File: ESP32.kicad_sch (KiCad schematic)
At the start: 29 parts, among them J1 USB_B_Micro, J2 BATT, J3 PMS7003 Connector, J4 BootSel, J5 UART, Q1 AO3401A, SW1 RESET, U1 ESP32-C3-MINI-1, U2 AMS1117-3.3, U3 AMS1117-5.0

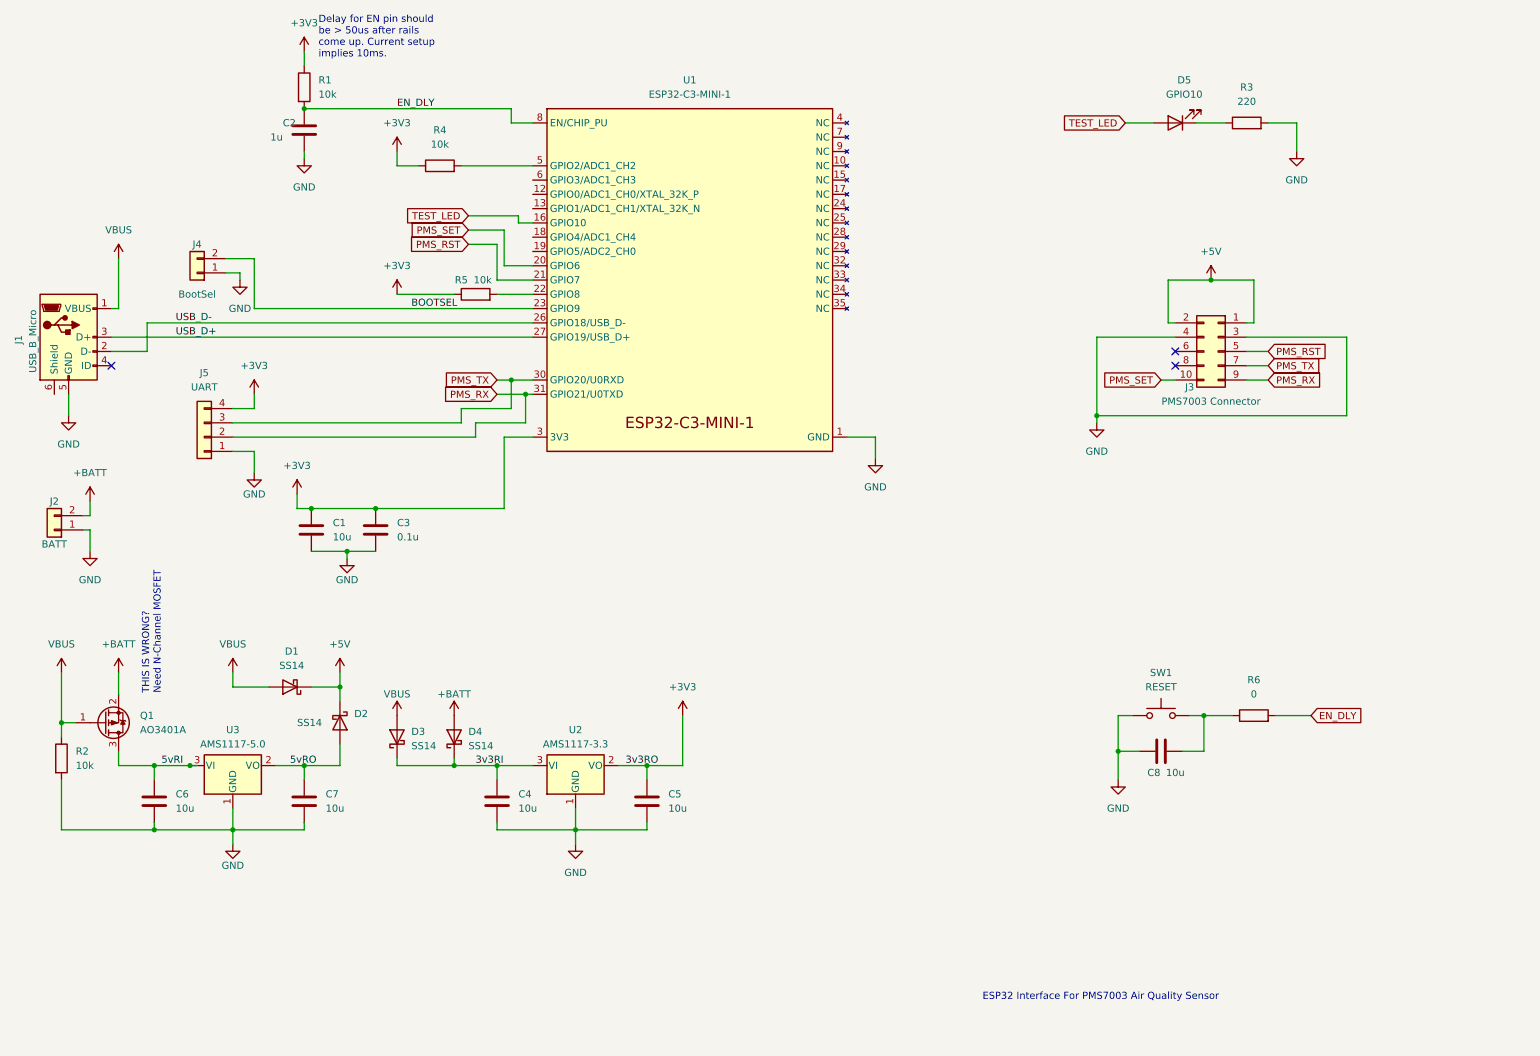
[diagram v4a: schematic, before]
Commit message: Sch layout + reroute
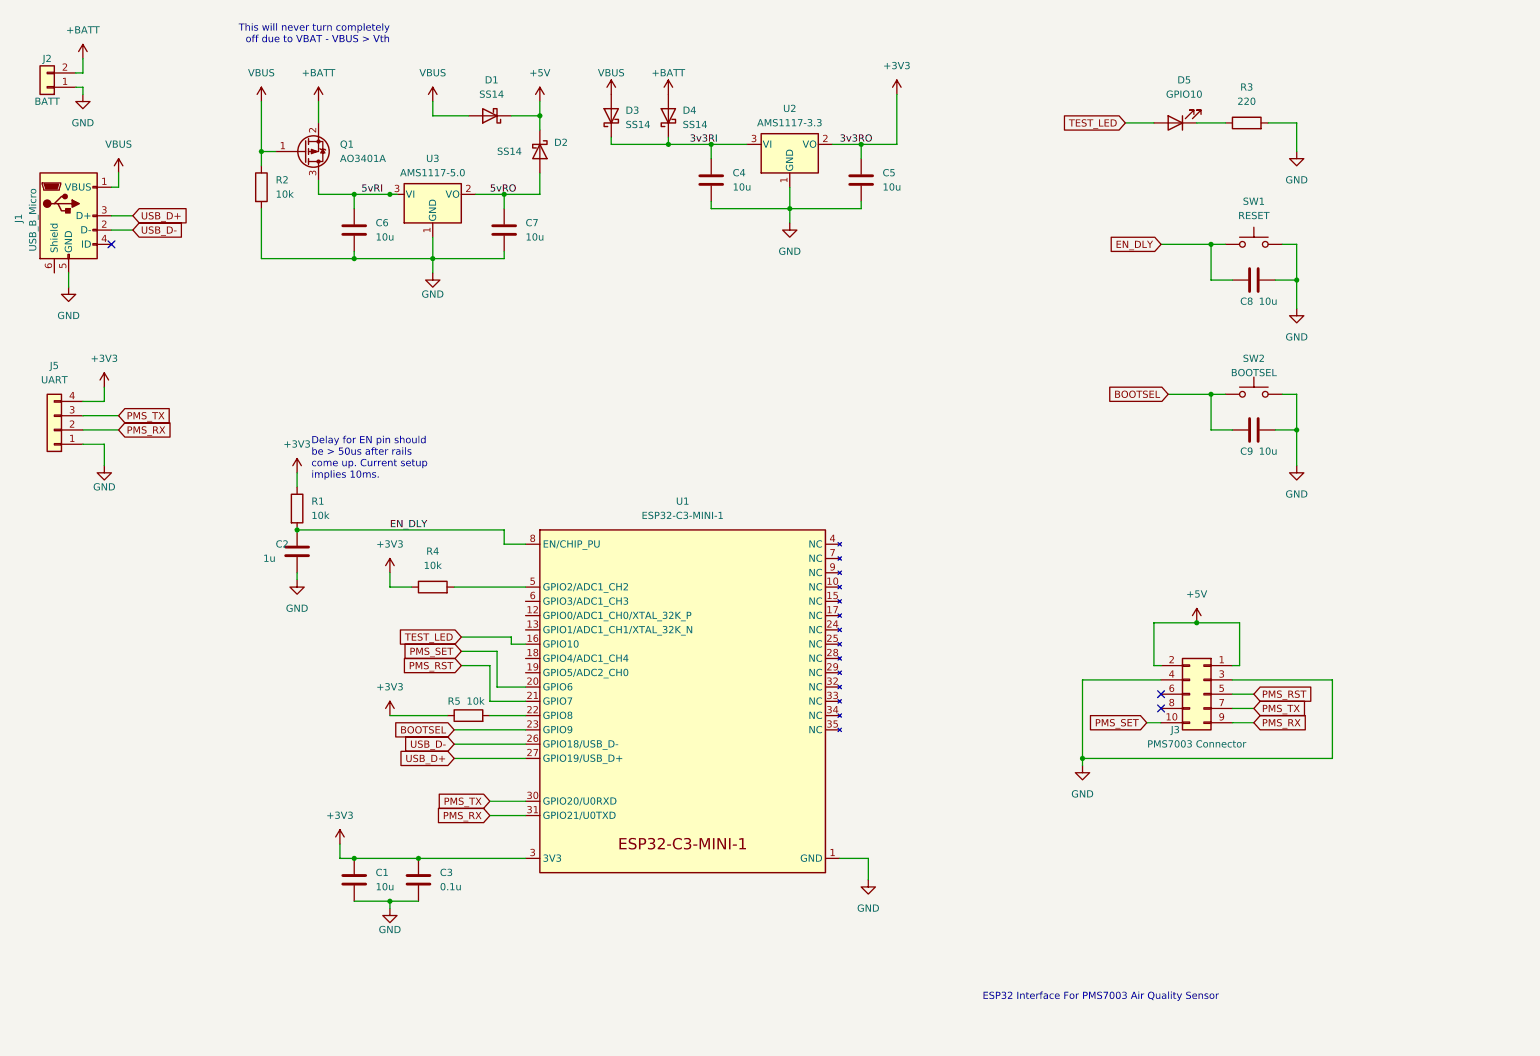
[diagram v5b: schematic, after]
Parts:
- removed J4: BootSel, Connector_PinHeader_2.54mm:PinHeader_1x02_P2.54mm_Vertical, symbol Connector_Generic:Conn_01x02
- removed R6: 0, Resistor_SMD:R_0603_1608Metric_Pad0.98x0.95mm_HandSolder, symbol Device:R
- added C9: 10u, Capacitor_SMD:C_0603_1608Metric_Pad1.08x0.95mm_HandSolder, symbol Device:C
- added SW2: BOOTSEL, Button_Switch_SMD:SW_Push_1P1T_NO_Vertical_Wuerth_434133025816, symbol Switch:SW_Push
- J2: footprint Connector_PinHeader_2.54mm:PinHeader_1x02_P2.54mm_Vertical -> Connector_PinHeader_2.54mm:PinHeader_1x02_P2.54mm_Vertical_SMD_Pin1Right
- J5: footprint Connector_PinHeader_2.54mm:PinHeader_1x04_P2.54mm_Vertical -> Connector_PinHeader_2.54mm:PinHeader_1x04_P2.54mm_Vertical_SMD_Pin1Right
- SW1: footprint Button_Switch_THT:SW_PUSH_6mm -> Button_Switch_SMD:SW_Push_1P1T_NO_Vertical_Wuerth_434133025816
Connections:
- net BOOTSEL: now also C9.1, SW2.1
- net EN_DLY: now also C8.1, SW1.1
- net GND: now also C8.2, SW1.2, C9.2, SW2.2; no longer C8.1, SW1.1
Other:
- note added: "This will never turn completely off due to VBAT - VBUS > Vth"
- note removed: "THIS IS WRONG? Need N-Channel MOSFET"
- moved on the sheet: C1, C2, C3, C4, C5, C6, C7, C8, D1, D2, D3, D4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

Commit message: Replaced linear regulators with buck converters
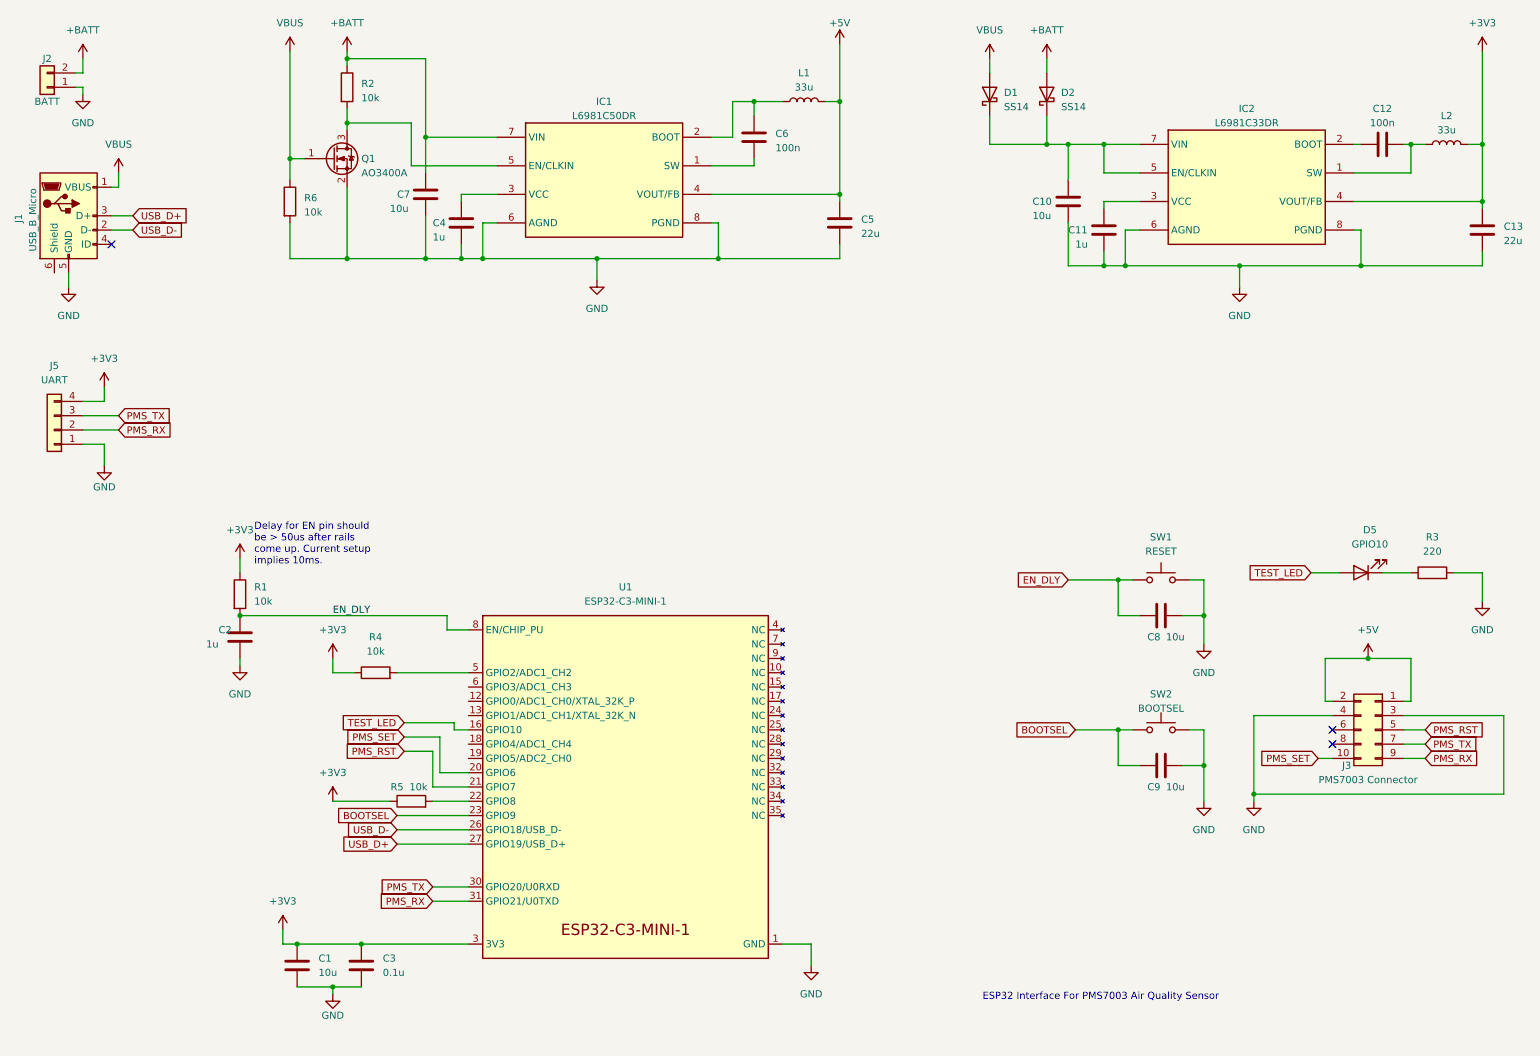
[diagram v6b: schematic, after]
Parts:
- removed D3, D4: SS14, Diode_SMD:D_SMA_Handsoldering, symbol Device:D_Schottky
- removed Q1: AO3401A, Package_TO_SOT_SMD:SOT-23, symbol Transistor_FET:AO3401A
- removed U2: AMS1117-3.3, Package_TO_SOT_SMD:SOT-223-3_TabPin2, symbol Regulator_Linear:AMS1117-3.3
- removed U3: AMS1117-5.0, Package_TO_SOT_SMD:SOT-223-3_TabPin2, symbol Regulator_Linear:AMS1117-5.0
- added C10: 10u, Capacitor_SMD:C_0603_1608Metric_Pad1.08x0.95mm_HandSolder, symbol Device:C
- added C11: 1u, Capacitor_SMD:C_0603_1608Metric_Pad1.08x0.95mm_HandSolder, symbol Device:C
- added C12: 100n, Capacitor_SMD:C_0603_1608Metric_Pad1.08x0.95mm_HandSolder, symbol Device:C
- added C13: 22u, Capacitor_SMD:C_0603_1608Metric_Pad1.08x0.95mm_HandSolder, symbol Device:C
- added IC1: L6981C50DR, DC Converters:SOIC127P600X175-8N, symbol L6981C50DR:L6981C50DR
- added IC2: L6981C33DR, DC Converters:SOIC127P600X175-8N, symbol L6981C50DR:L6981C33DR
- added L1, L2: 33u, Inductor_SMD:L_Murata_29xxxC, symbol Device:L
- added Q1: AO3400A, Package_TO_SOT_SMD:SOT-23, symbol Transistor_FET:AO3400A
- added R6: 10k, Resistor_SMD:R_0603_1608Metric_Pad0.98x0.95mm_HandSolder, symbol Device:R
- C4: value 10u -> 1u; footprint Capacitor_SMD:C_1206_3216Metric_Pad1.33x1.80mm_HandSolder -> Capacitor_SMD:C_0603_1608Metric_Pad1.08x0.95mm_HandSolder
- C5: value 10u -> 22u; footprint Capacitor_Tantalum_SMD:CP_EIA-3216-18_Kemet-A_Pad1.58x1.35mm_HandSolder -> Capacitor_SMD:C_0603_1608Metric_Pad1.08x0.95mm_HandSolder
- C6: value 10u -> 100n; footprint Capacitor_SMD:C_1206_3216Metric_Pad1.33x1.80mm_HandSolder -> Capacitor_SMD:C_0603_1608Metric_Pad1.08x0.95mm_HandSolder
- C7: footprint Capacitor_Tantalum_SMD:CP_EIA-3216-18_Kemet-A_Pad1.58x1.35mm_HandSolder -> Capacitor_SMD:C_0603_1608Metric_Pad1.08x0.95mm_HandSolder
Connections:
- net 5vRO is gone; now on net +BATT: C7.1, D2.2 (A)
- net +3V3: now also C13.1, IC2.4 (VOUT/FB), L2.2; no longer C5.1
- net +5V: now also C5.1, IC1.4 (VOUT/FB), L1.2; no longer D1.1 (K), D2.1 (K)
- net +BATT: now also R2.1, IC1.7 (VIN)
- net GND: now also C10.2, C11.2, C13.2, IC1.6 (AGND), IC1.8 (PGND), IC2.6 (AGND), IC2.8 (PGND), Q1.2 (S), R6.2; no longer C6.2, R2.2
- net VBUS: now also Q1.1 (G), R6.1; no longer R2.1
- net 3v3RI: no longer names the net of C4.1
- net 3v3RI: now also IC1.3 (VCC)
- net 5vRI: no longer names the net of C6.1
- net 5vRI: now also IC1.1 (SW)
- new net: IC1.5 (EN/CLKIN), Q1.3 (D), R2.2
- new net: C10.1, D1.1 (K), D2.1 (K), IC2.5 (EN/CLKIN), IC2.7 (VIN)
- new net: C6.2, IC1.2 (BOOT), L1.1
- new net: C12.2, IC2.1 (SW), L2.1
- new net: C12.1, IC2.2 (BOOT)
- new net: C11.1, IC2.3 (VCC)
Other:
- note removed: "This will never turn completely off due to VBAT - VBUS > Vth"
- moved on the sheet: C1, C2, C3, C8, C9, D5, J3, R1, R3, R4, R5, SW1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

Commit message: Schematic + Layout
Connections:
- net PMS_RX: now also J3.7 (Pin_7); no longer J3.9 (Pin_9)
- net PMS_TX: now also J3.9 (Pin_9); no longer J3.7 (Pin_7)
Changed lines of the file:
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@@
+    (stroke (width 0) (type default))
+  )
+  (wire (pts (xy 261.62 147.32) (xy 265.43 147.32))
     (stroke (width 0) (type default))
   )
@@
     (stroke (width 0) (type default))
   )
-  (wire (pts (xy 261.62 147.32) (xy 265.43 147.32))
-    (stroke (width 0) (type default))
-  )
   (wire (pts (xy 71.12 132.08) (xy 74.93 132.08))
     (stroke (width 0) (type default))
@@
     (stroke (width 0) (type default))
   )
+  (wire (pts (xy 261.62 144.78) (xy 265.43 144.78))
+    (stroke (width 0) (type default))
+  )
   (wire (pts (xy 257.81 114.3) (xy 262.89 114.3))
     (stroke (width 0) (type default))
@@
   )
   (wire (pts (xy 30.48 83.82) (xy 30.48 81.28))
-    (stroke (width 0) (type default))
-  )
-  (wire (pts (xy 261.62 144.78) (xy 265.43 144.78))
     (stroke (width 0) (type default))
   )
@@
     )
   )
-  (global_label "PMS_RX" (shape input) (at 265.43 147.32 0) (fields_autoplaced)
-    (effects (font (size 1.27 1.27)) (justify left))
-    (property "Intersheetrefs" "${INTERSHEET_REFS}" (at 275.2212 147.2406 0)
+  (global_label "PMS_RX" (shape input) (at 265.43 144.78 0) (fields_autoplaced)
+    (effects (font (size 1.27 1.27)) (justify left))
+    (property "Intersheetrefs" "${INTERSHEET_REFS}" (at 275.2212 144.7006 0)
       (effects (font (size 1.27 1.27)) (justify left) hide)
     )
@@
     )
   )
-  (global_label "PMS_TX" (shape input) (at 265.43 144.78 0) (fields_autoplaced)
-    (effects (font (size 1.27 1.27)) (justify left))
-    (property "Intersheetrefs" "${INTERSHEET_REFS}" (at 274.9188 144.7006 0)
-      (effects (font (size 1.27 1.27)) (justify left) hide)
-    )
+  (global_label "PMS_TX" (shape input) (at 265.43 147.32 0) (fields_autoplaced)
+    (effects (font (size 1.27 1.27)) (justify left))
+    (property "Intersheetrefs" "${INTERSHEET_REFS}" (at 274.9188 147.2406 0)
+      (effects (font (size 1.27 1.27)) (justify left) hide)
+    )
